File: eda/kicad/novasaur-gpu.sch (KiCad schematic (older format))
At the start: 21 parts, among them U1 74F86, U28 74F163, U29 74F163, U3 74F08, U30 74F541, U31 74F574, U32 74F574, U33 74F541, U34 74F574, U35 74F299, U36 74F574, U37 74F157

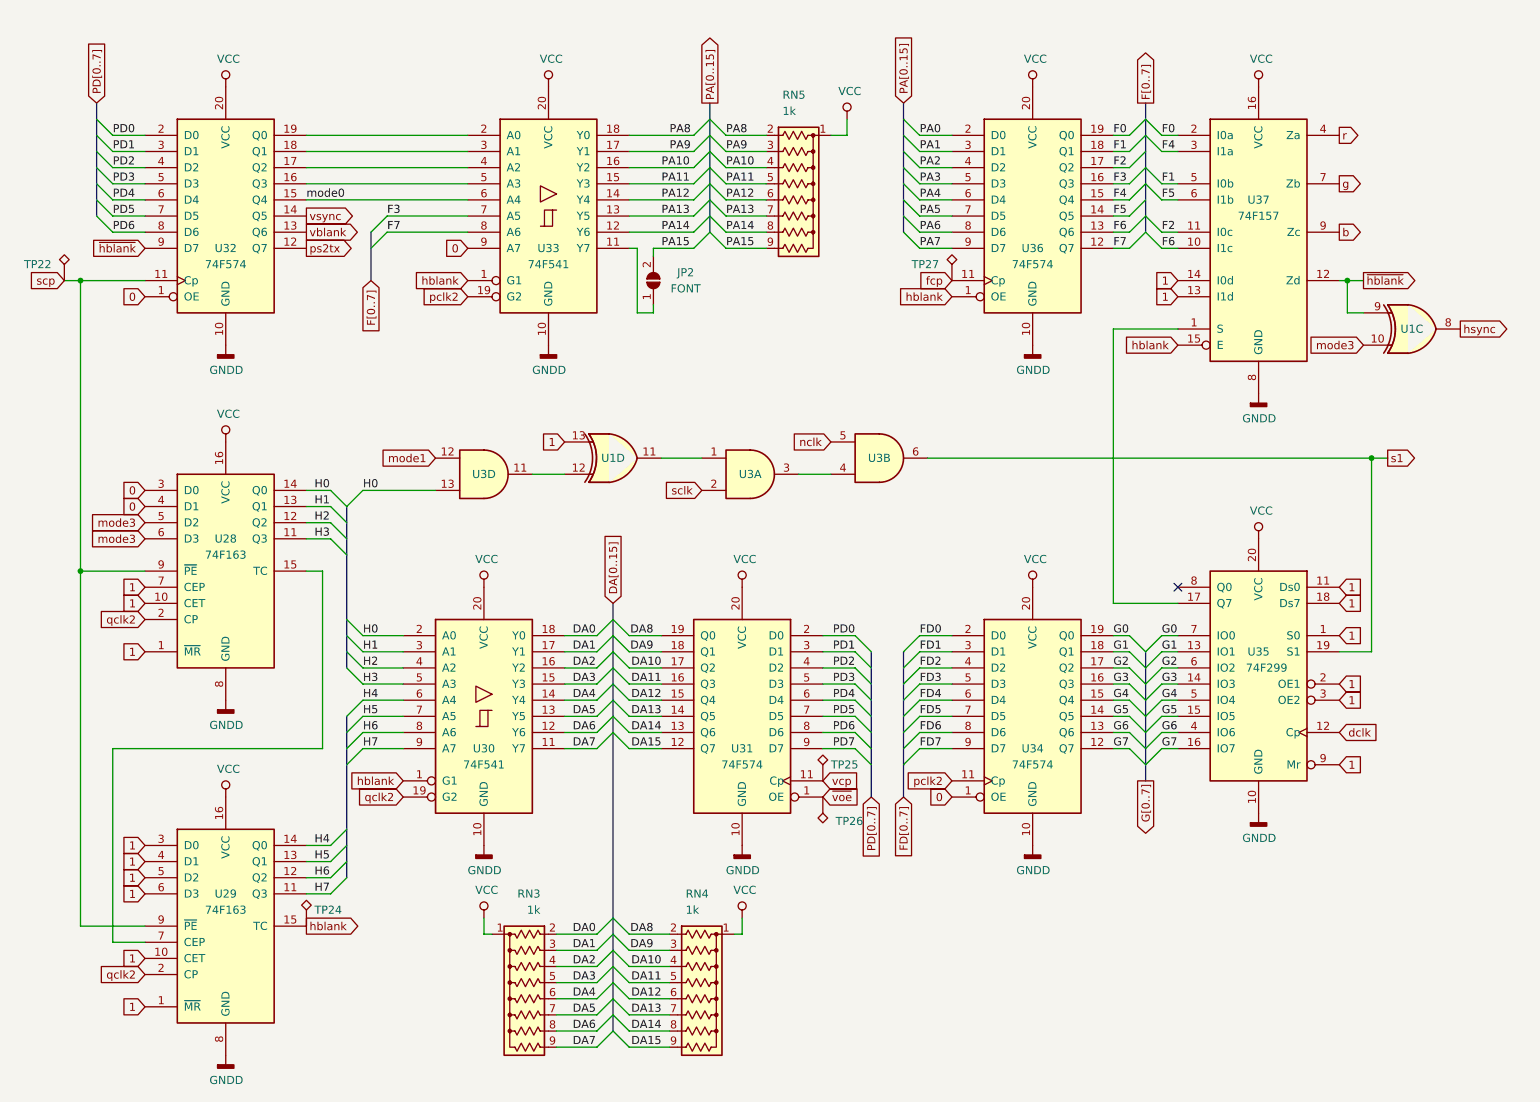
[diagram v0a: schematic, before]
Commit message: add dedicated ps2 clock enable line Use mode0|1 to select VDAC using DRL
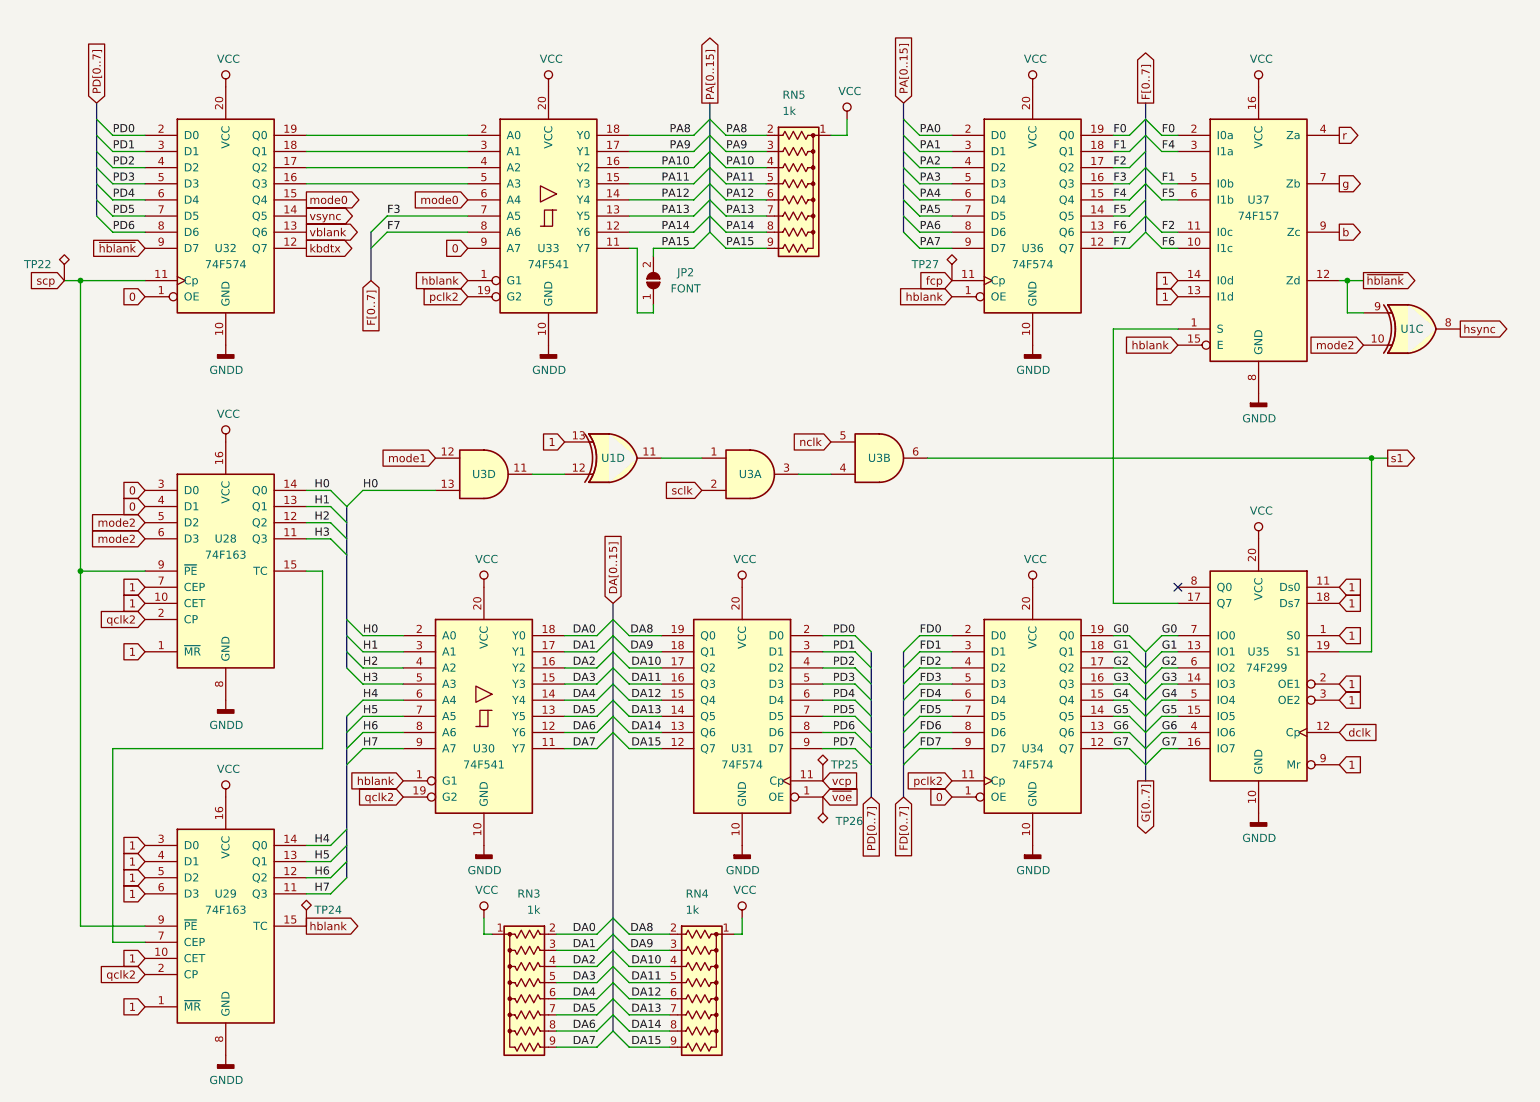
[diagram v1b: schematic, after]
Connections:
- net mode3 renamed mode2
- net ps2tx renamed kbdtx
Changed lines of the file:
@@
 Sheet 3 4
 Title "Graphics Processing Unit"
-Date "2020-07-18"
+Date "2020-08-20"
 Rev "1.7"
 Comp ""
@@
 0
 Text GLabel 1650 3950 0    50   Input ~ 0
-mode3
+mode2
 Text GLabel 1650 3750 0    50   Input ~ 0
 0
 Text GLabel 1650 4050 0    50   Input ~ 0
-mode3
+mode2
 Wire Wire Line
 	2650 4250 2750 4250
@@
 $EndComp
 Text GLabel 9200 2850 0    50   Input ~ 0
-mode3
+mode2
 Text GLabel 1650 4750 0    50   Input ~ 0
 1
@@
 Wire Wire Line
 	9250 3550 9250 4750
-Wire Wire Line
-	2650 1950 3650 1950
 Text GLabel 4250 3450 0    50   Input ~ 0
 1
@@
 Wire Wire Line
 	4850 3550 5100 3550
-Text Label 2650 1950 0    50   ~ 0
-mode0
 Text GLabel 1650 2250 0    50   Input ~ 0
 ~hblank
 Text GLabel 2650 2250 2    50   Output ~ 0
-ps2tx
+kbdtx
 $Comp
 L Connector:TestPoint_Alt TP?
@@
 Text GLabel 9200 2450 2    50   Output ~ 0
 ~hblank
+Text GLabel 2650 1950 2    50   Output ~ 0
+mode0
+Text GLabel 3650 1950 0    50   Input ~ 0
+mode0
 Wire Bus Line
 	3050 2150 3050 2450

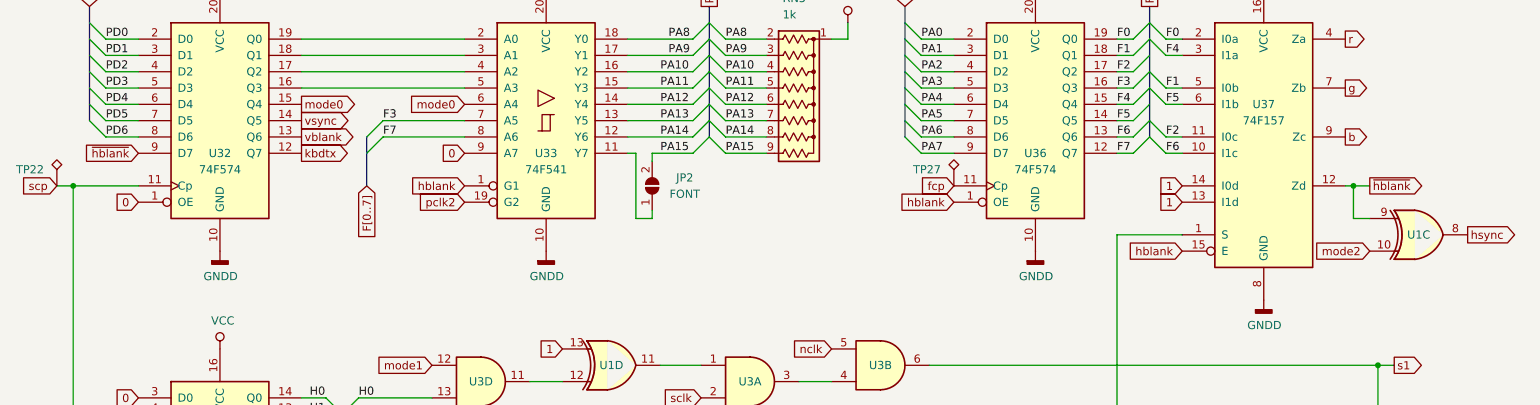
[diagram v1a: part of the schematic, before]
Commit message: refactor comms Add keyboard scan jump page, overload tx mode state to select keyboard jump page
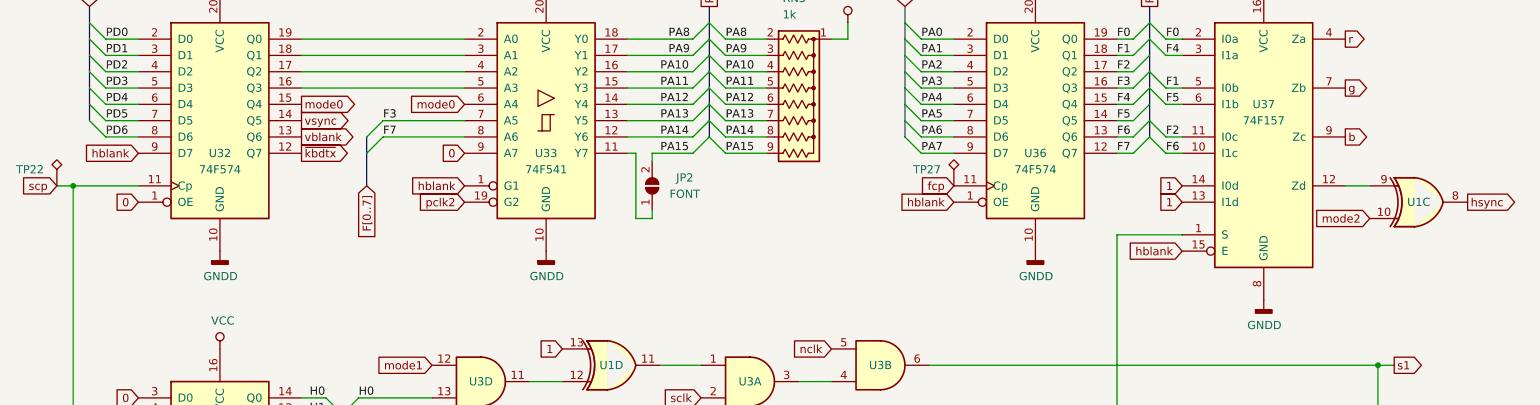
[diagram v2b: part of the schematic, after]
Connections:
- net hblank: now also U32.9 (D7)
- net kbdtx renamed ~kbdtx
- net ~hblank: no longer names the net of U1.9, U37.12 (Zd)
- net ~hblank: no longer U32.9 (D7)
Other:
- moved on the sheet: U1C
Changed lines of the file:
@@
 	1    0    0    -1
 $EndComp
-Text GLabel 9200 2850 0    50   Input ~ 0
+Text GLabel 9200 2650 0    50   Input ~ 0
 mode2
 Text GLabel 1650 4750 0    50   Input ~ 0
@@
 L 74xx:74LS86 U?
 U 3 1 5E79B6AD
-P 9500 2750
+P 9500 2550
 AR Path="/5E79B6AD" Ref="U?"  Part="3"
 AR Path="/5DA1E9BD/5E79B6AD" Ref="U1"  Part="3"
-F 0 "U1" H 9500 2750 50  0000 C CNN
-F 1 "74F86" H 9500 2984 50  0001 C CNN
-F 2 "Package_DIP:DIP-14_W7.62mm_LongPads" H 9500 2750 50  0001 C CNN
-F 3 "74xx/74ls86.pdf" H 9500 2750 50  0001 C CNN
-	3    9500 2750
+F 0 "U1" H 9500 2550 50  0000 C CNN
+F 1 "74F86" H 9500 2784 50  0001 C CNN
+F 2 "Package_DIP:DIP-14_W7.62mm_LongPads" H 9500 2550 50  0001 C CNN
+F 3 "74xx/74ls86.pdf" H 9500 2550 50  0001 C CNN
+	3    9500 2550
 	1    0    0    -1
 $EndComp
-Text GLabel 9800 2750 2    50   Output ~ 0
+Text GLabel 9800 2550 2    50   Output ~ 0
 hsync
-Wire Wire Line
-	9050 2450 9100 2450
 Wire Wire Line
 	5700 3650 5900 3650
@@
 	4850 3550 5100 3550
 Text GLabel 1650 2250 0    50   Input ~ 0
-~hblank
+hblank
 Text GLabel 2650 2250 2    50   Output ~ 0
-kbdtx
+~kbdtx
 $Comp
 L Connector:TestPoint_Alt TP?
@@
 	1250 2450 1650 2450
 Connection ~ 1250 2450
-Wire Wire Line
-	9200 2650 9100 2650
-Wire Wire Line
-	9100 2650 9100 2450
-Connection ~ 9100 2450
-Wire Wire Line
-	9100 2450 9200 2450
-Text GLabel 9200 2450 2    50   Output ~ 0
-~hblank
 Text GLabel 2650 1950 2    50   Output ~ 0
 mode0
 Text GLabel 3650 1950 0    50   Input ~ 0
 mode0
+Wire Wire Line
+	9050 2450 9200 2450
 Wire Bus Line
 	3050 2150 3050 2450

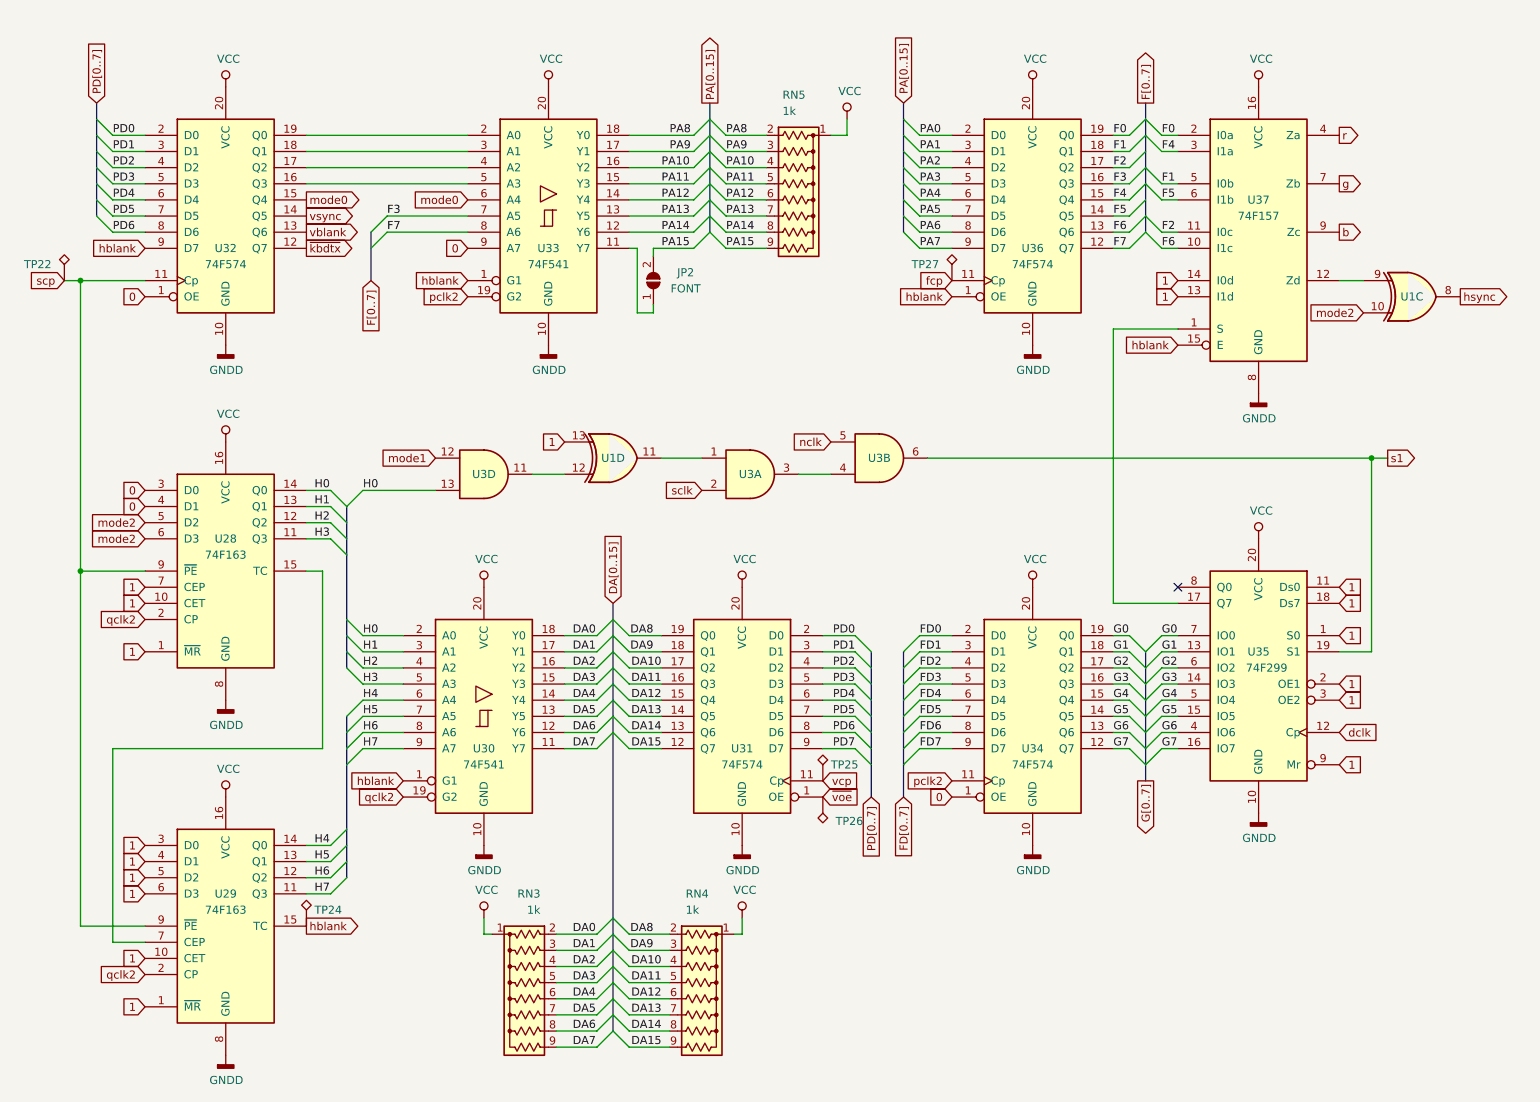
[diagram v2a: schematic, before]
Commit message: finish up HAL Completed versions of comms: FORKH forks based on top 3 bits within (000) audio (001) rx (010) tx (011) kbd pages Rx is started by RMODE 1 - asserts RTS and fills buffer, deasserts RTS when buffer full, times out after RTO process cycles of stop bits Tx is started by TMODE 2 - ends if CTS asserted or end of buffer, interupted by adding 1 to TMODE Kbd is branched from the Tx thread, started from Tx and ends after fixed process cycle timeout (TBD)
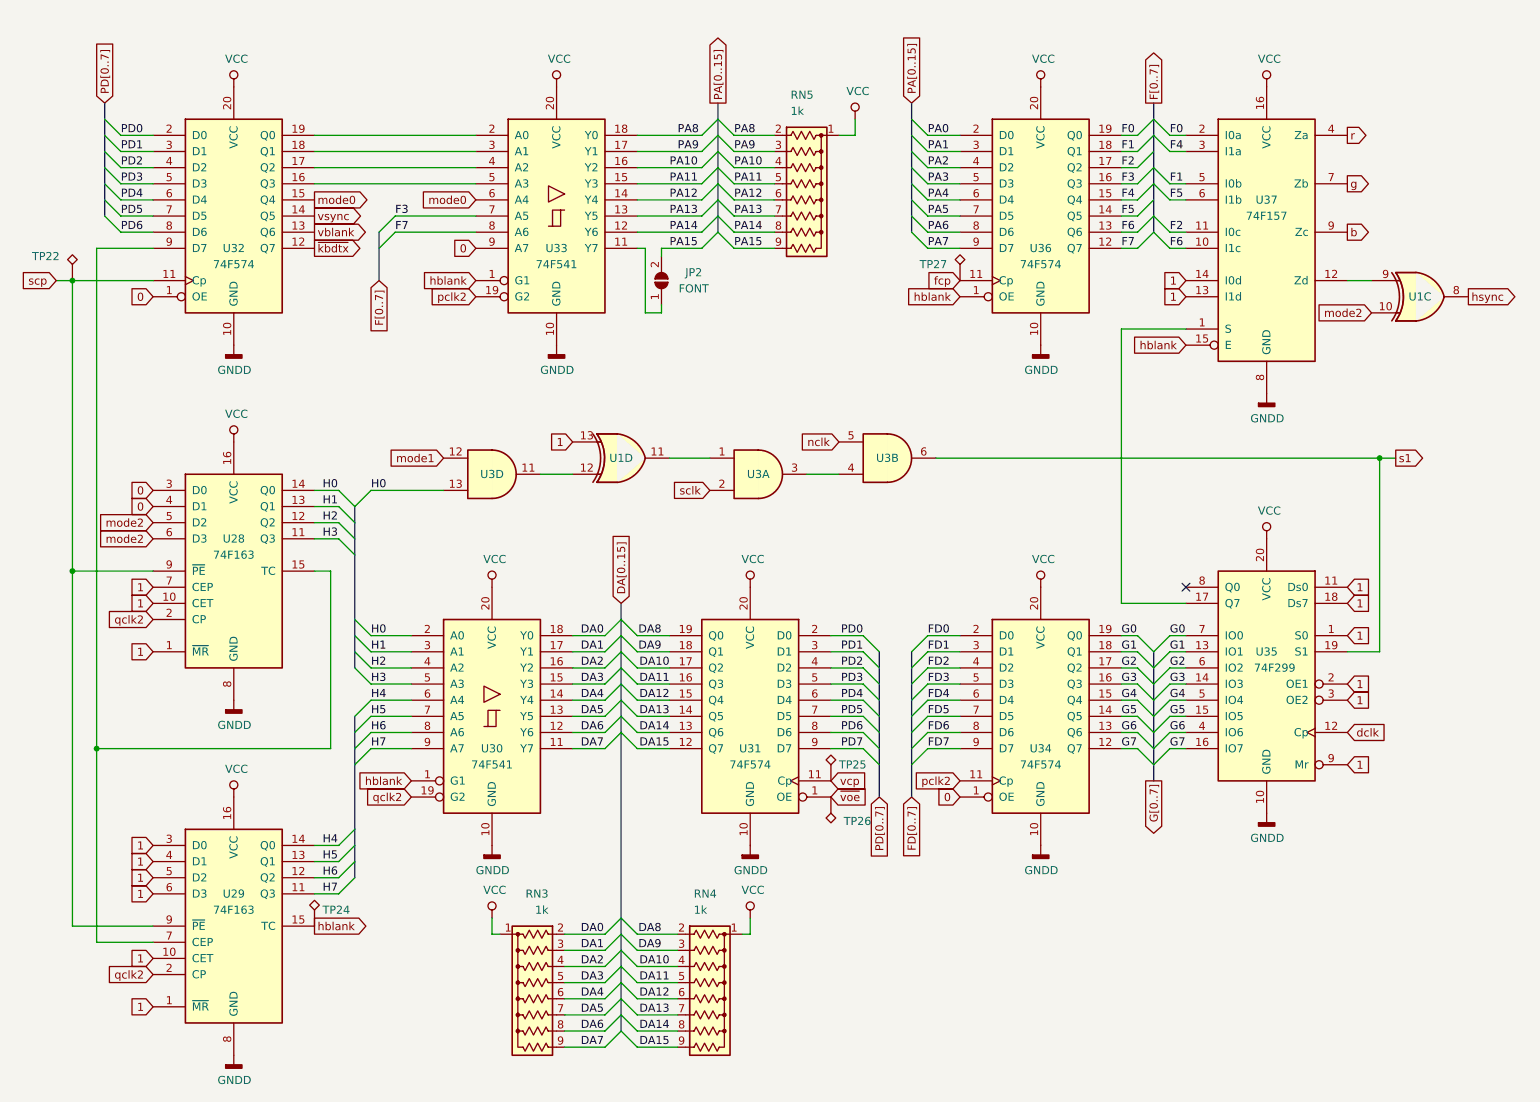
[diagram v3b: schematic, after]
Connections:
- net hblank: no longer U32.9 (D7)
- net at U28.15 (TC), U29.7 (CEP): now also U32.9 (D7)
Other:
- moved on the sheet: JP2, RN3, RN4, RN5, TP22, TP24, TP25, TP26, TP27, U1C, U1D, U28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
